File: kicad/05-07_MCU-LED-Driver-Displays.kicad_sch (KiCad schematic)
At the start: 66 parts, among them J5 Conn_02x05_Counter_Clockwise, J6 Conn_01x13_Pin, J7 Conn_01x03_Pin, J8 Conn_01x03_Pin, Q4 AO3400A, Q5 AO3400A, SW1 B3U-1100PM, SW2 BOOTSEL, SW3 RESET, SW4 USER_A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

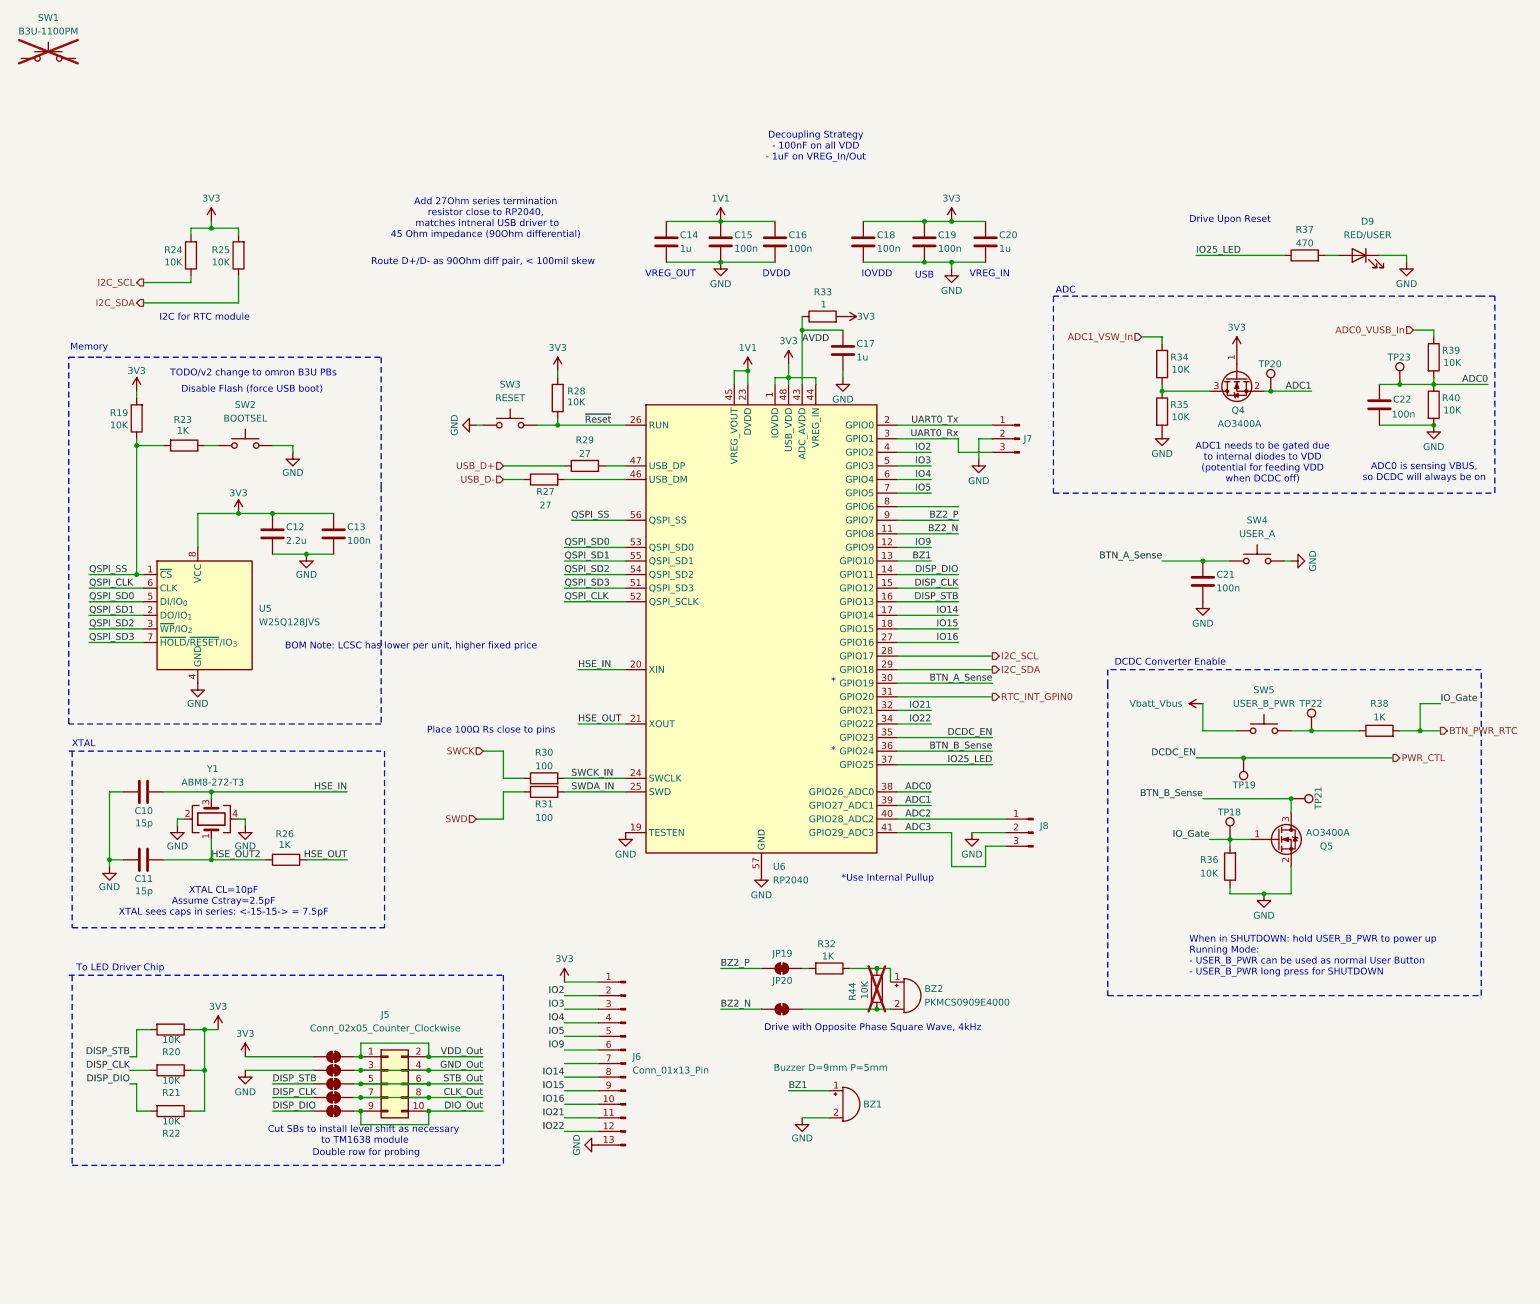
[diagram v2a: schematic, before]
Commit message: layout - footprints update - may have corrupted kicad_sch project lib
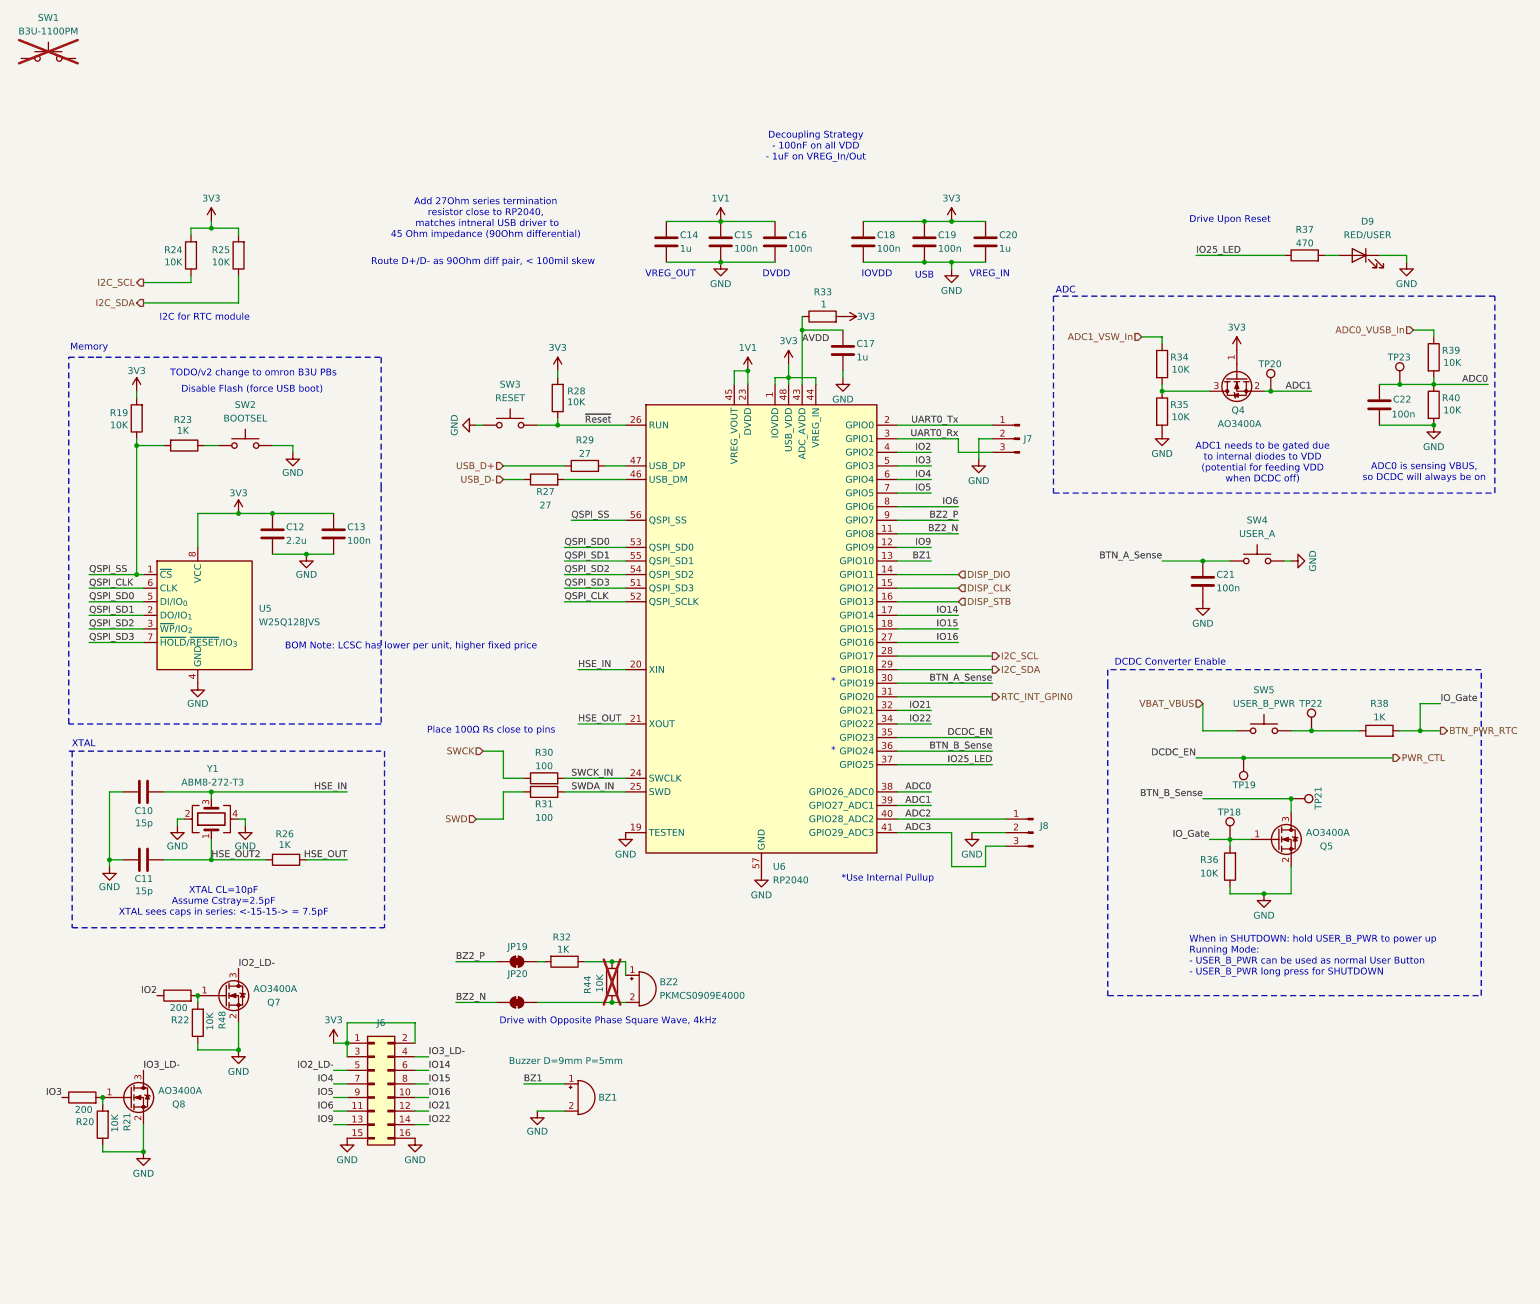
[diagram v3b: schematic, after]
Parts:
- removed J5: Conn_02x05_Counter_Clockwise, Connector_PinHeader_2.54mm:PinHeader_2x05_P2.54mm_Vertical, symbol Connector_Generic:Conn_02x05_Odd_Even
- removed J6: Conn_01x13_Pin, Connector_PinHeader_2.54mm:PinHeader_1x13_P2.54mm_Vertical, symbol Connector:Conn_01x13_Pin
- removed JP14, JP15, JP16, JP17, JP18: SolderJumper_2_Bridged, Jumper:SolderJumper-2_P1.3mm_Bridged_RoundedPad1.0x1.5mm, symbol Jumper:SolderJumper_2_Bridged
- added J6: Conn_02x08_Counter_Clockwise, Connector_PinHeader_2.54mm:PinHeader_2x07_P2.54mm_Vertical, symbol Connector_Generic:Conn_02x08_Odd_Even
- added Q7, Q8: AO3400A, Package_TO_SOT_SMD:SOT-23, symbol Transistor_FET:AO3400A
- added R48: 10K, Resistor_SMD:R_0805_2012Metric_Pad1.20x1.40mm_HandSolder, symbol Device:R
- R20, R22: value 10K -> 200
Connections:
- net 3V3: now also J6.1 (Pin_1), J6.2 (Pin_2), J6.3 (Pin_3); no longer R20.1, R21.1, R22.1
- net DISP_CLK: no longer R21.2
- net DISP_DIO: no longer R22.2
- net DISP_STB: no longer R20.2
- net GND: now also R21.1, J6.15 (Pin_15), J6.16 (Pin_16), Q7.2 (S), Q8.2 (S), R48.1
- net IO14: now also J6.6 (Pin_6)
- net IO15: now also J6.8 (Pin_8)
- net IO16: now also J6.10 (Pin_10)
- net IO2: now also R22.1
- net IO21: now also J6.12 (Pin_12)
- net IO22: now also J6.14 (Pin_14)
- net IO3: now also R20.1
- net IO4: now also J6.7 (Pin_7)
- net IO5: now also J6.9 (Pin_9)
- net IO9: now also J6.13 (Pin_13)
- net IO6: now reaches U6.8 (GPIO6)
- net IO6: now also J6.11 (Pin_11)
- net Vbatt_Vbus renamed VBAT_VBUS
- new net: Q8.1 (G), R20.2, R21.2
- new net: Q7.1 (G), R22.2, R48.2
- new net IO2_LD-: J6.5 (Pin_5), Q7.3 (D)
- new net IO3_LD-: J6.4 (Pin_4), Q8.3 (D)
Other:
- note removed: "Cut SBs to install level shift as necessary"
- note removed: "Double row for probing"
- note removed: "To LED Driver Chip"
- note removed: "to TM1638 module"
- moved on the sheet: BZ1, BZ2, JP19, JP20, R32, R44

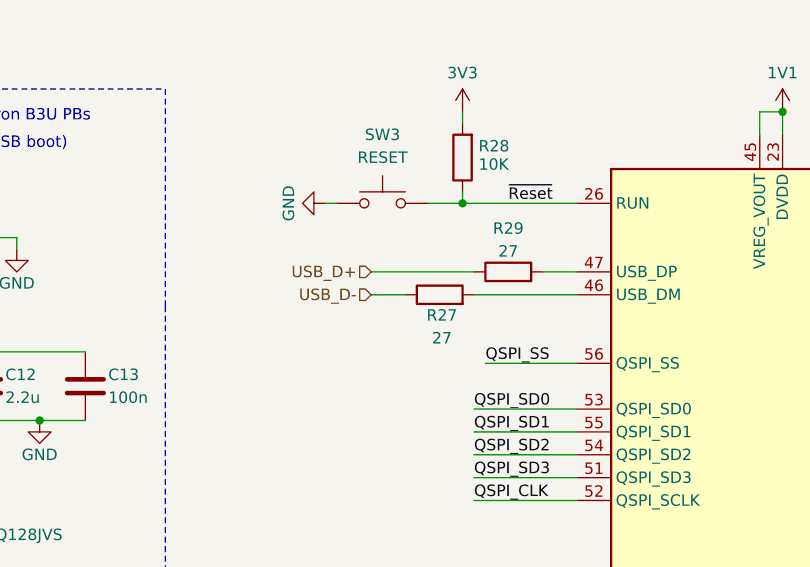
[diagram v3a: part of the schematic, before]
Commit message: start routing diff pairs
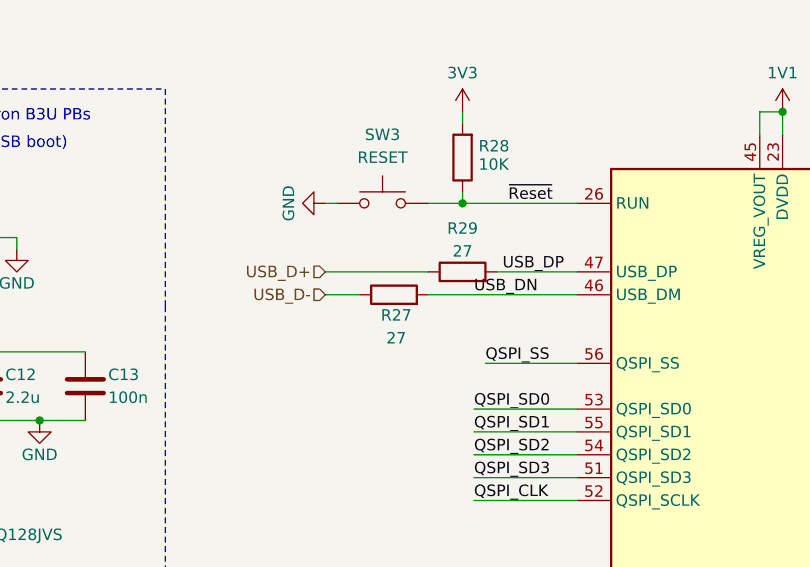
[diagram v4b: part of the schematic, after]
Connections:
- net USB_DN: now reaches R27.2, U6.46 (USB_DM)
- net USB_DP: now reaches R29.2, U6.47 (USB_DP)
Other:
- moved on the sheet: R27, R29
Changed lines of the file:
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@@
 	(wire
 		(pts
-			(xy 99.06 67.31) (xy 102.87 67.31)
+			(xy 93.98 67.31) (xy 97.79 67.31)
 		)
 		(stroke
@@
 	(wire
 		(pts
-			(xy 118.11 64.77) (xy 121.92 64.77)
+			(xy 113.03 64.77) (xy 121.92 64.77)
 		)
 		(stroke
@@
 	(wire
 		(pts
-			(xy 110.49 67.31) (xy 121.92 67.31)
+			(xy 105.41 67.31) (xy 121.92 67.31)
 		)
 		(stroke
@@
 	(wire
 		(pts
-			(xy 99.06 64.77) (xy 110.49 64.77)
+			(xy 93.98 64.77) (xy 105.41 64.77)
 		)
 		(stroke
@@
 		)
 	)
+	(label "USB_DP"
+		(at 113.665 64.77 0)
+		(effects
+			(font
+				(size 1.27 1.27)
+			)
+			(justify left bottom)
+		)
+	)
 	(label "ADC1"
 		(at 179.07 128.27 180)
@@
 		)
 	)
+	(label "USB_DN"
+		(at 110.49 67.31 0)
+		(effects
+			(font
+				(size 1.27 1.27)
+			)
+			(justify left bottom)
+		)
+	)
 	(label "BTN_A_Sense"
 		(at 222.25 82.55 180)
@@
 	(hierarchical_label "USB_D-"
 		(shape input)
-		(at 99.06 67.31 180)
+		(at 93.98 67.31 180)
 		(effects
 			(font
@@
 	(hierarchical_label "USB_D+"
 		(shape input)
-		(at 99.06 64.77 180)
+		(at 93.98 64.77 180)
 		(effects
 			(font
@@
 	(symbol
 		(lib_id "Device:R")
-		(at 106.68 67.31 90)
+		(at 101.6 67.31 90)
 		(unit 1)
 		(exclude_from_sim no)
@@
 		(dnp no)
 		(property "Reference" "R27"
-			(at 106.934 69.596 90)
+			(at 101.854 69.596 90)
 			(effects
 				(font
@@
 		)
 		(property "Value" "27"
-			(at 106.934 72.136 90)
+			(at 101.854 72.136 90)
 			(effects
 				(font
@@
 		)
 		(property "Footprint" "Resistor_SMD:R_0805_2012Metric_Pad1.20x1.40mm_HandSolder"
-			(at 106.68 69.088 90)
+			(at 101.6 69.088 90)
 			(effects
 				(font
@@
 		)
 		(property "Datasheet" "~"
-			(at 106.68 67.31 0)
+			(at 101.6 67.31 0)
 			(effects
 				(font
@@
 		)
 		(property "Description" "Resistor"
-			(at 106.68 67.31 0)
+			(at 101.6 67.31 0)
 			(effects
 				(font
@@
 		)
 		(property "Subsystem" "06-MCU-IO"
-			(at 106.68 67.31 90)
+			(at 101.6 67.31 90)
 			(effects
 				(font
@@
 		)
 		(property "MPN" "(Generic)"
-			(at 106.68 67.31 90)
+			(at 101.6 67.31 90)
 			(effects
 				(font
@@
 		)
 		(property "Manufacturer" "(Generic)"
-			(at 106.68 67.31 90)
+			(at 101.6 67.31 90)
 			(effects
 				(font
@@
 		)
 		(property "Supplier 1" "(Generic)"
-			(at 106.68 67.31 90)
+			(at 101.6 67.31 90)
 			(effects
 				(font
@@
 		)
 		(property "Package" "0805"
-			(at 106.68 67.31 90)
+			(at 101.6 67.31 90)
 			(effects
 				(font
@@
 	(symbol
 		(lib_id "Device:R")
-		(at 114.3 64.77 90)
+		(at 109.22 64.77 90)
 		(unit 1)
 		(exclude_from_sim no)
@@
 		(dnp no)
 		(property "Reference" "R29"
-			(at 114.3 59.944 90)
+			(at 109.22 59.944 90)
 			(effects
 				(font
@@
 		)
 		(property "Value" "27"
-			(at 114.3 62.484 90)
+			(at 109.22 62.484 90)
 			(effects
 				(font
@@
 		)
 		(property "Footprint" "Resistor_SMD:R_0805_2012Metric_Pad1.20x1.40mm_HandSolder"
-			(at 114.3 66.548 90)
+			(at 109.22 66.548 90)
 			(effects
 				(font
@@
 		)
 		(property "Datasheet" "~"
-			(at 114.3 64.77 0)
+			(at 109.22 64.77 0)
 			(effects
 				(font
@@
 		)
 		(property "Description" "Resistor"
-			(at 114.3 64.77 0)
+			(at 109.22 64.77 0)
 			(effects
 				(font
@@
 		)
 		(property "Subsystem" "06-MCU-IO"
-			(at 114.3 64.77 90)
+			(at 109.22 64.77 90)
 			(effects
 				(font
@@
 		)
 		(property "MPN" "(Generic)"
-			(at 114.3 64.77 90)
+			(at 109.22 64.77 90)
 			(effects
 				(font
@@
 		)
 		(property "Manufacturer" "(Generic)"
-			(at 114.3 64.77 90)
+			(at 109.22 64.77 90)
 			(effects
 				(font
@@
 		)
 		(property "Supplier 1" "(Generic)"
-			(at 114.3 64.77 90)
+			(at 109.22 64.77 90)
 			(effects
 				(font
@@
 		)
 		(property "Package" "0805"
-			(at 114.3 64.77 90)
+			(at 109.22 64.77 90)
 			(effects
 				(font

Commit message: changed usb port, prepare first bom export
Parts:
- BZ1, C10, C11, C12, C13, C14, C15, C16, C17, C18, C19, C20, C21, C22, J6, J7, J8, SW1, SW2, SW3, SW4, SW5: Lab_In_Stock (none) -> Y
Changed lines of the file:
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@@
 			)
 		)
+		(property "Lab_In_Stock" "Y"
+			(at 177.8 22.86 0)
+			(effects
+				(font
+					(size 1.27 1.27)
+				)
+				(hide yes)
+			)
+		)
 		(pin "2"
 		)
@@
 			)
 		)
+		(property "Lab_In_Stock" "Y"
+			(at 262.89 53.34 0)
+			(effects
+				(font
+					(size 1.27 1.27)
+				)
+				(hide yes)
+			)
+		)
 		(pin "2"
 		)
@@
 			)
 		)
+		(property "Lab_In_Stock" "Y"
+			(at 195.58 59.69 0)
+			(effects
+				(font
+					(size 1.27 1.27)
+				)
+				(hide yes)
+			)
+		)
 		(pin "1"
 		)
@@
 			)
 		)
+		(property "Lab_In_Stock" "Y"
+			(at 139.7 22.86 0)
+			(effects
+				(font
+					(size 1.27 1.27)
+				)
+				(hide yes)
+			)
+		)
 		(pin "2"
 		)
@@
 			)
 		)
+		(property "Lab_In_Stock" "Y"
+			(at 31.75 125.73 90)
+			(effects
+				(font
+					(size 1.27 1.27)
+				)
+				(hide yes)
+			)
+		)
 		(pin "2"
 		)
@@
 			)
 		)
+		(property "Lab_In_Stock" "Y"
+			(at 74.93 180.34 0)
+			(effects
+				(font
+					(size 1.27 1.27)
+				)
+				(hide yes)
+			)
+		)
 		(pin "4"
 		)
@@
 			)
 		)
+		(property "Lab_In_Stock" "Y"
+			(at 189.23 22.86 0)
+			(effects
+				(font
+					(size 1.27 1.27)
+				)
+				(hide yes)
+			)
+		)
 		(pin "2"
 		)
@@
 			)
 		)
+		(property "Lab_In_Stock" "Y"
+			(at 100.33 57.15 0)
+			(effects
+				(font
+					(size 1.27 1.27)
+				)
+				(hide yes)
+			)
+		)
 		(pin "1"
 		)
@@
 			)
 		)
+		(property "Lab_In_Stock" "Y"
+			(at 129.54 22.86 0)
+			(effects
+				(font
+					(size 1.27 1.27)
+				)
+				(hide yes)
+			)
+		)
 		(pin "2"
 		)
@@
 			)
 		)
+		(property "Lab_In_Stock" "Y"
+			(at 166.37 22.86 0)
+			(effects
+				(font
+					(size 1.27 1.27)
+				)
+				(hide yes)
+			)
+		)
 		(pin "2"
 		)
@@
 			)
 		)
+		(property "Lab_In_Stock" "Y"
+			(at 241.3 114.3 0)
+			(effects
+				(font
+					(size 1.27 1.27)
+				)
+				(hide yes)
+			)
+		)
 		(pin "1"
 		)
@@
 			)
 		)
+		(property "Lab_In_Stock" "Y"
+			(at 149.86 22.86 0)
+			(effects
+				(font
+					(size 1.27 1.27)
+				)
+				(hide yes)
+			)
+		)
 		(pin "2"
 		)
@@
 			)
 		)
+		(property "Lab_In_Stock" "Y"
+			(at 13.97 -11.43 0)
+			(effects
+				(font
+					(size 1.27 1.27)
+				)
+				(hide yes)
+			)
+		)
 		(pin "1"
 		)
@@
 			)
 		)
+		(property "Lab_In_Stock" "Y"
+			(at 229.87 86.36 0)
+			(effects
+				(font
+					(size 1.27 1.27)
+				)
+				(hide yes)
+			)
+		)
 		(pin "2"
 		)
@@
 			)
 		)
+		(property "Lab_In_Stock" "Y"
+			(at 113.03 182.88 0)
+			(effects
+				(font
+					(size 1.27 1.27)
+				)
+				(hide yes)
+			)
+		)
 		(pin "1"
 		)
@@
 			)
 		)
+		(property "Lab_In_Stock" "Y"
+			(at 55.88 77.47 0)
+			(effects
+				(font
+					(size 1.27 1.27)
+				)
+				(hide yes)
+			)
+		)
 		(pin "2"
 		)
@@
 			)
 		)
+		(property "Lab_In_Stock" "Y"
+			(at 162.56 43.18 0)
+			(effects
+				(font
+					(size 1.27 1.27)
+				)
+				(hide yes)
+			)
+		)
 		(pin "2"
 		)
@@
 			)
 		)
+		(property "Lab_In_Stock" "Y"
+			(at 31.75 138.43 90)
+			(effects
+				(font
+					(size 1.27 1.27)
+				)
+				(hide yes)
+			)
+		)
 		(pin "2"
 		)
@@
 			)
 		)
+		(property "Lab_In_Stock" "Y"
+			(at 67.31 77.47 0)
+			(effects
+				(font
+					(size 1.27 1.27)
+				)
+				(hide yes)
+			)
+		)
 		(pin "2"
 		)
@@
 			)
 		)
+		(property "Lab_In_Stock" "Y"
+			(at 198.12 133.35 0)
+			(effects
+				(font
+					(size 1.27 1.27)
+				)
+				(hide yes)
+			)
+		)
 		(pin "1"
 		)
@@
 			)
 		)
+		(property "Lab_In_Stock" "Y"
+			(at 240.03 82.55 0)
+			(effects
+				(font
+					(size 1.27 1.27)
+				)
+				(hide yes)
+			)
+		)
 		(pin "1"
 		)
@@
 			(at 50.8 60.96 0)
 			(effects
+				(font
+					(size 1.27 1.27)
+				)
+				(hide yes)
+			)
+		)
+		(property "Lab_In_Stock" "Y"
+			(at 50.8 60.96 0)
+			(effects
